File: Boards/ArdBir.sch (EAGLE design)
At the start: 30 parts, among them IC2 LM2940

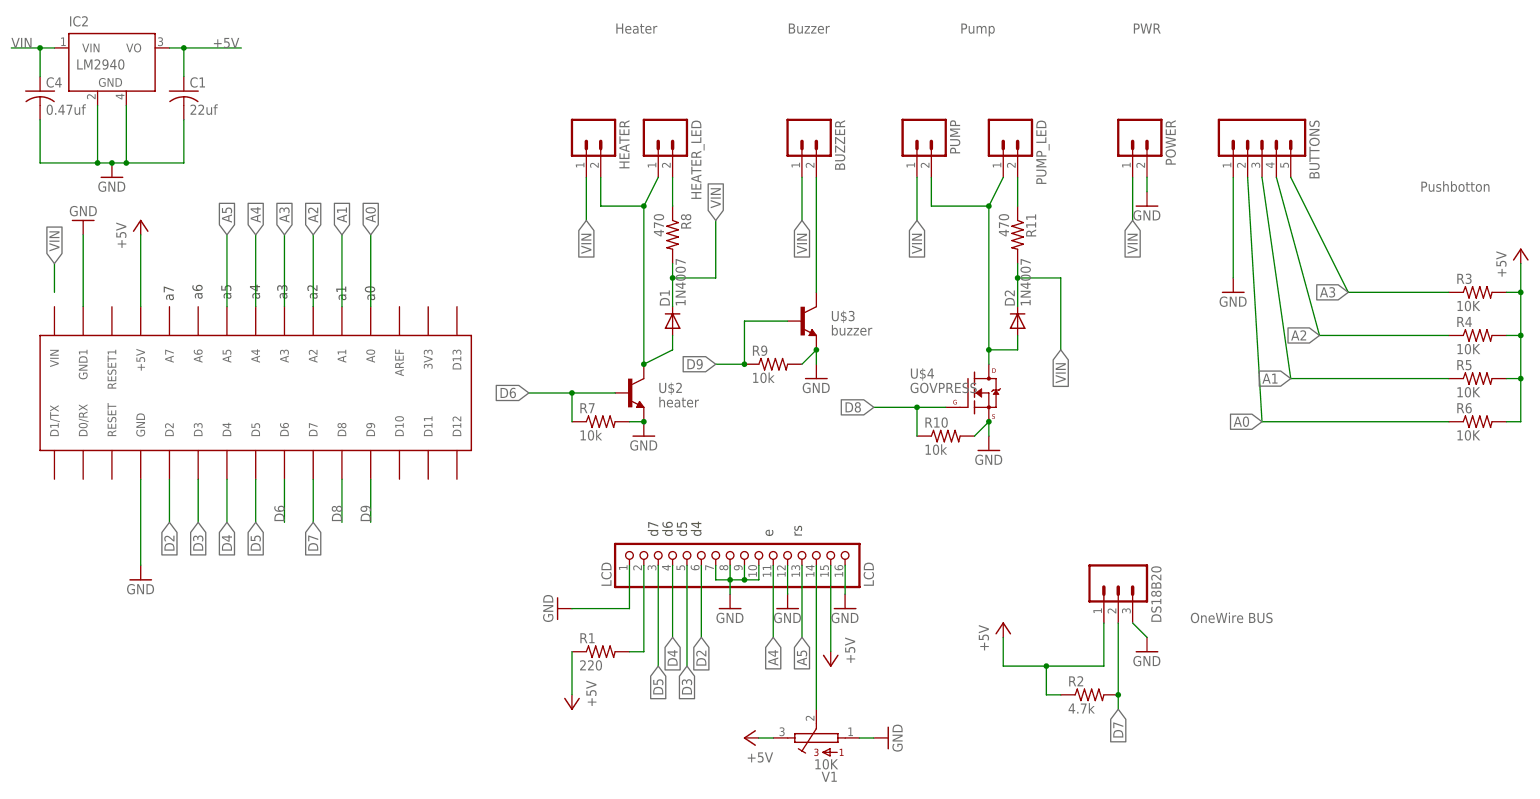
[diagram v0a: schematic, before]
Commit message: Added part numbers for MOSFETs
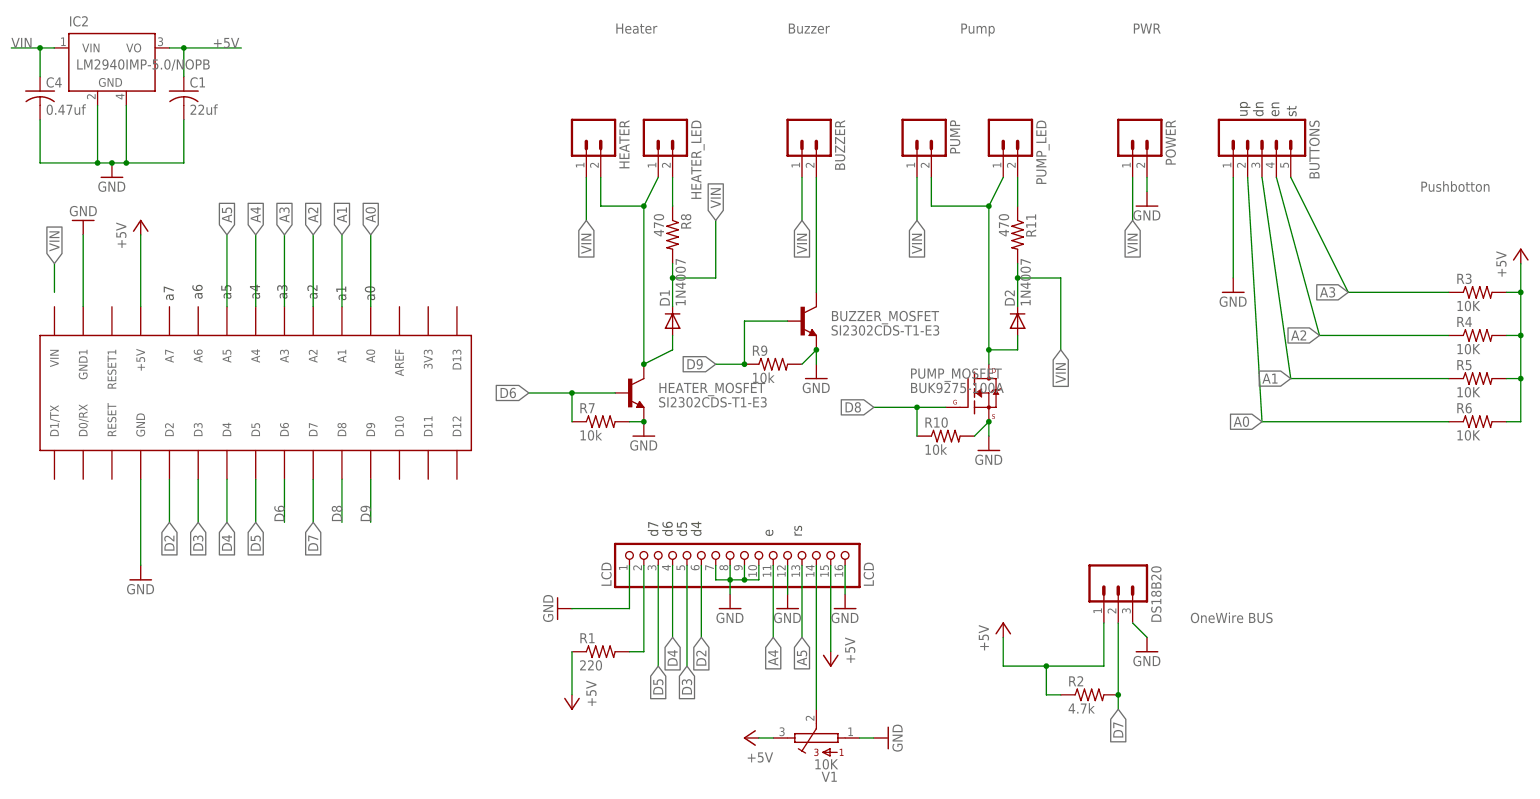
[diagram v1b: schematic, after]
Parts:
- BUZZER_MOSFET: value buzzer -> SI2302CDS-T1-E3
- HEATER_MOSFET: value heater -> SI2302CDS-T1-E3
- IC2: value LM2940 -> LM2940IMP-5.0/NOPB
- PUMP_MOSFET: value GOVPRESS -> BUK9275-100A
- renumbered U$2 to HEATER_MOSFET, U$3 to BUZZER_MOSFET, U$4 to PUMP_MOSFET
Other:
- note added: "dn"
- note added: "en"
- note added: "st"
- note added: "up"
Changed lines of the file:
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@@
 </part>
 <part name="U$1" library="jet-lib" deviceset="ARDUINONANO" device=""/>
-<part name="U$2" library="SparkFun" deviceset="TRANSISTOR_NPN" device="SOT23" value="heater"/>
+<part name="HEATER_MOSFET" library="SparkFun" deviceset="TRANSISTOR_NPN" device="SOT23" value="SI2302CDS-T1-E3"/>
 <part name="R7" library="adafruit" deviceset="R-US_" device="R0805" value="10k"/>
 <part name="R9" library="adafruit" deviceset="R-US_" device="R0805" value="10k"/>
@@
 <part name="DS18B20" library="SparkFun" deviceset="M03" device="LONGPADS"/>
 <part name="BUTTONS" library="SparkFun" deviceset="M05" device="LOCK"/>
-<part name="U$3" library="SparkFun" deviceset="TRANSISTOR_NPN" device="SOT23" value="buzzer"/>
+<part name="BUZZER_MOSFET" library="SparkFun" deviceset="TRANSISTOR_NPN" device="SOT23" value="SI2302CDS-T1-E3"/>
 <part name="HEATER_LED" library="SparkFun" deviceset="M02" device="LOCK"/>
 <part name="PUMP_LED" library="SparkFun" deviceset="M02" device="LOCK"/>
@@
 <part name="GND14" library="supply1" deviceset="GND" device=""/>
 <part name="C4" library="rcl" deviceset="C-US" device="C0805" value="0.47uf"/>
-<part name="IC2" library="national-semiconductor" deviceset="LM2936MP?*" device="" technology="-5.0" value="LM2940"/>
+<part name="IC2" library="national-semiconductor" deviceset="LM2936MP?*" device="" technology="-5.0" value="LM2940IMP-5.0/NOPB"/>
 <part name="C1" library="rcl" deviceset="C-US" device="C0805" value="22uf"/>
-<part name="U$4" library="dpak" deviceset="BUK9275-100A" device="" value="GOVPRESS"/>
+<part name="PUMP_MOSFET" library="dpak" deviceset="BUK9275-100A" device="" value="BUK9275-100A"/>
 </parts>
 <sheets>
@@
 <text x="-6.858" y="80.01" size="1.778" layer="97" rot="R90">a6</text>
 <text x="-11.938" y="79.756" size="1.778" layer="97" rot="R90">a7</text>
+<text x="177.8" y="112.268" size="1.778" layer="97" rot="R90">up</text>
+<text x="180.594" y="112.268" size="1.778" layer="97" rot="R90">dn</text>
+<text x="183.388" y="112.268" size="1.778" layer="97" rot="R90">en</text>
+<text x="186.436" y="112.268" size="1.778" layer="97" rot="R90">st</text>
 </plain>
 <instances>
@@
 </instance>
 <instance part="U$1" gate="G$1" x="-35.56" y="53.34" rot="R90"/>
-<instance part="U$2" gate="G$1" x="68.58" y="63.5"/>
+<instance part="HEATER_MOSFET" gate="G$1" x="68.58" y="63.5"/>
 <instance part="R7" gate="G$1" x="63.5" y="58.42"/>
 <instance part="R9" gate="G$1" x="93.98" y="68.58"/>
@@
 <instance part="DS18B20" gate="G$1" x="154.94" y="30.48" rot="R270"/>
 <instance part="BUTTONS" gate="G$1" x="180.34" y="109.22" rot="R270"/>
-<instance part="U$3" gate="G$1" x="99.06" y="76.2"/>
+<instance part="BUZZER_MOSFET" gate="G$1" x="99.06" y="76.2"/>
 <instance part="HEATER_LED" gate="G$1" x="73.66" y="109.22" rot="R270"/>
 <instance part="PUMP_LED" gate="G$1" x="134.62" y="109.22" rot="R270"/>
@@
 <instance part="IC2" gate="G$1" x="-22.86" y="121.92"/>
 <instance part="C1" gate="G$1" x="-10.16" y="116.84"/>
-<instance part="U$4" gate="G$1" x="129.54" y="63.5"/>
+<instance part="PUMP_MOSFET" gate="G$1" x="129.54" y="63.5"/>
 </instances>
 <busses>
@@
 <pinref part="R9" gate="G$1" pin="2"/>
 <wire x1="99.06" y1="68.58" x2="101.6" y2="71.12" width="0.1524" layer="91"/>
-<pinref part="U$3" gate="G$1" pin="E"/>
+<pinref part="BUZZER_MOSFET" gate="G$1" pin="E"/>
 <wire x1="101.6" y1="71.12" x2="101.6" y2="68.58" width="0.1524" layer="91"/>
 </segment>
@@
 <pinref part="R10" gate="G$1" pin="2"/>
 <wire x1="129.54" y1="55.88" x2="132.08" y2="58.42" width="0.1524" layer="91"/>
-<pinref part="U$4" gate="G$1" pin="S"/>
+<pinref part="PUMP_MOSFET" gate="G$1" pin="S"/>
 <junction x="132.08" y="58.42"/>
 <wire x1="132.08" y1="58.42" x2="132.08" y2="55.88" width="0.1524" layer="91"/>
@@
 <pinref part="R7" gate="G$1" pin="2"/>
 <wire x1="68.58" y1="58.42" x2="71.12" y2="58.42" width="0.1524" layer="91"/>
-<pinref part="U$2" gate="G$1" pin="E"/>
+<pinref part="HEATER_MOSFET" gate="G$1" pin="E"/>
 </segment>
 <segment>
@@
 <pinref part="R10" gate="G$1" pin="1"/>
 <wire x1="119.38" y1="60.96" x2="119.38" y2="55.88" width="0.1524" layer="91"/>
-<pinref part="U$4" gate="G$1" pin="G"/>
+<pinref part="PUMP_MOSFET" gate="G$1" pin="G"/>
 </segment>
 <segment>
@@
 <wire x1="88.9" y1="68.58" x2="88.9" y2="76.2" width="0.1524" layer="91"/>
 <wire x1="88.9" y1="76.2" x2="96.52" y2="76.2" width="0.1524" layer="91"/>
-<pinref part="U$3" gate="G$1" pin="B"/>
+<pinref part="BUZZER_MOSFET" gate="G$1" pin="B"/>
 </segment>
 <segment>
@@
 <pinref part="D1" gate="G$1" pin="A"/>
 <wire x1="76.2" y1="71.12" x2="76.2" y2="73.66" width="0.1524" layer="91"/>
-<pinref part="U$2" gate="G$1" pin="C"/>
+<pinref part="HEATER_MOSFET" gate="G$1" pin="C"/>
 <junction x="71.12" y="68.58"/>
 <pinref part="HEATER_LED" gate="G$1" pin="1"/>
@@
 <segment>
 <wire x1="101.6" y1="101.6" x2="101.6" y2="81.28" width="0.1524" layer="91"/>
-<pinref part="U$3" gate="G$1" pin="C"/>
+<pinref part="BUZZER_MOSFET" gate="G$1" pin="C"/>
 <pinref part="BUZZER" gate="G$1" pin="2"/>
 </segment>
@@
 <pinref part="PUMP_LED" gate="G$1" pin="1"/>
 <pinref part="PUMP" gate="G$1" pin="2"/>
-<pinref part="U$4" gate="G$1" pin="D"/>
+<pinref part="PUMP_MOSFET" gate="G$1" pin="D"/>
 </segment>
 </net>
@@
 <pinref part="R7" gate="G$1" pin="1"/>
 <wire x1="58.42" y1="63.5" x2="58.42" y2="58.42" width="0.1524" layer="91"/>
-<pinref part="U$2" gate="G$1" pin="B"/>
-</segment>
-<segment>
+<pinref part="HEATER_MOSFET" gate="G$1" pin="B"/>
+</segment>
+<segment>
